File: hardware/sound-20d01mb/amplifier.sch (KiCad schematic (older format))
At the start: 43 parts

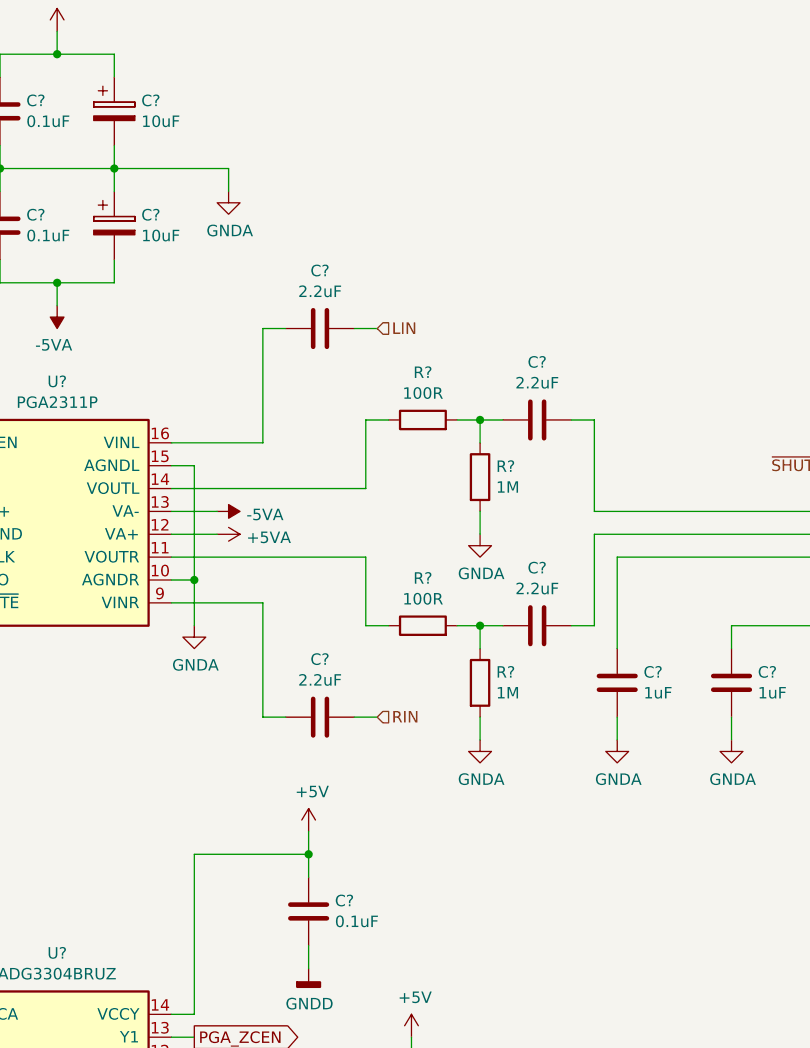
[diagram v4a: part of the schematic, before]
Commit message: Updated amplifier.sch
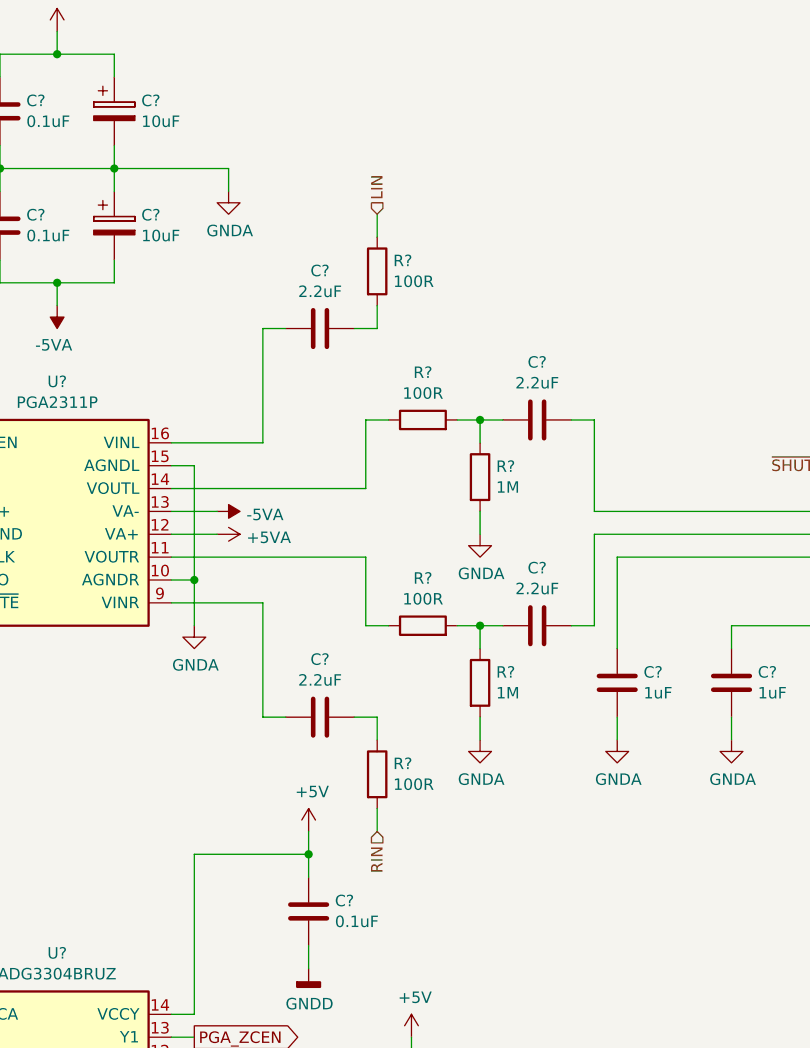
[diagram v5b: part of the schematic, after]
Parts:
- added R? (x2): 100R, Resistor_SMD:R_1206_3216Metric_Pad1.42x1.75mm_HandSolder, symbol Device:R
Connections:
- net LIN: now also R?.1; no longer C?.2
- net RIN: now also R?.2; no longer C?.2
- new net: C?.2, R?.2
- new net: C?.2, R?.1
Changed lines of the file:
@@
 	0    -1   -1   0
 $EndComp
-Text HLabel 4150 2700 2    50   Input ~ 0
+Text HLabel 4150 2200 1    50   Input ~ 0
 LIN
-Text HLabel 4150 4400 2    50   Input ~ 0
+Text HLabel 4150 4900 3    50   Input ~ 0
 RIN
 Text HLabel 10350 3000 2    50   Output ~ 0
@@
 	3650 4400 3750 4400
 Wire Wire Line
-	4150 2700 4050 2700
-Wire Wire Line
-	4150 4400 4050 4400
-Wire Wire Line
 	3250 3400 4100 3400
 Wire Wire Line
@@
 Wire Wire Line
 	5100 3600 6450 3600
+$Comp
+L Device:R R?
+U 1 1 60E82F70
+P 4150 2450
+F 0 "R?" H 4220 2496 50  0000 L CNN
+F 1 "100R" H 4220 2405 50  0000 L CNN
+F 2 "Resistor_SMD:R_1206_3216Metric_Pad1.42x1.75mm_HandSolder" V 4080 2450 50  0001 C CNN
+F 3 "~" H 4150 2450 50  0001 C CNN
+	1    4150 2450
+	1    0    0    -1
+$EndComp
+Wire Wire Line
+	4150 2200 4150 2300
+Wire Wire Line
+	4150 2600 4150 2700
+Wire Wire Line
+	4150 2700 4050 2700
+$Comp
+L Device:R R?
+U 1 1 60E9DE19
+P 4150 4650
+F 0 "R?" H 4220 4696 50  0000 L CNN
+F 1 "100R" H 4220 4605 50  0000 L CNN
+F 2 "Resistor_SMD:R_1206_3216Metric_Pad1.42x1.75mm_HandSolder" V 4080 4650 50  0001 C CNN
+F 3 "~" H 4150 4650 50  0001 C CNN
+	1    4150 4650
+	1    0    0    -1
+$EndComp
+Wire Wire Line
+	4150 4900 4150 4800
+Wire Wire Line
+	4150 4500 4150 4400
+Wire Wire Line
+	4150 4400 4050 4400
 $EndSCHEMATC

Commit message: THT to SMD Capacitor (2)
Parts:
- C?: footprint Capacitor_THT:CP_Radial_D8.0mm_P3.50mm -> Capacitor_SMD:CP_Elec_4x5.4
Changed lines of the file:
@@
 F 0 "C?" H 1268 2296 50  0000 L CNN
 F 1 "10uF" H 1268 2205 50  0000 L CNN
-F 2 "Capacitor_THT:CP_Radial_D8.0mm_P3.50mm" H 1188 2100 50  0001 C CNN
+F 2 "Capacitor_SMD:CP_Elec_4x5.4" H 1188 2100 50  0001 C CNN
 F 3 "~" H 1150 2250 50  0001 C CNN
 	1    1150 2250

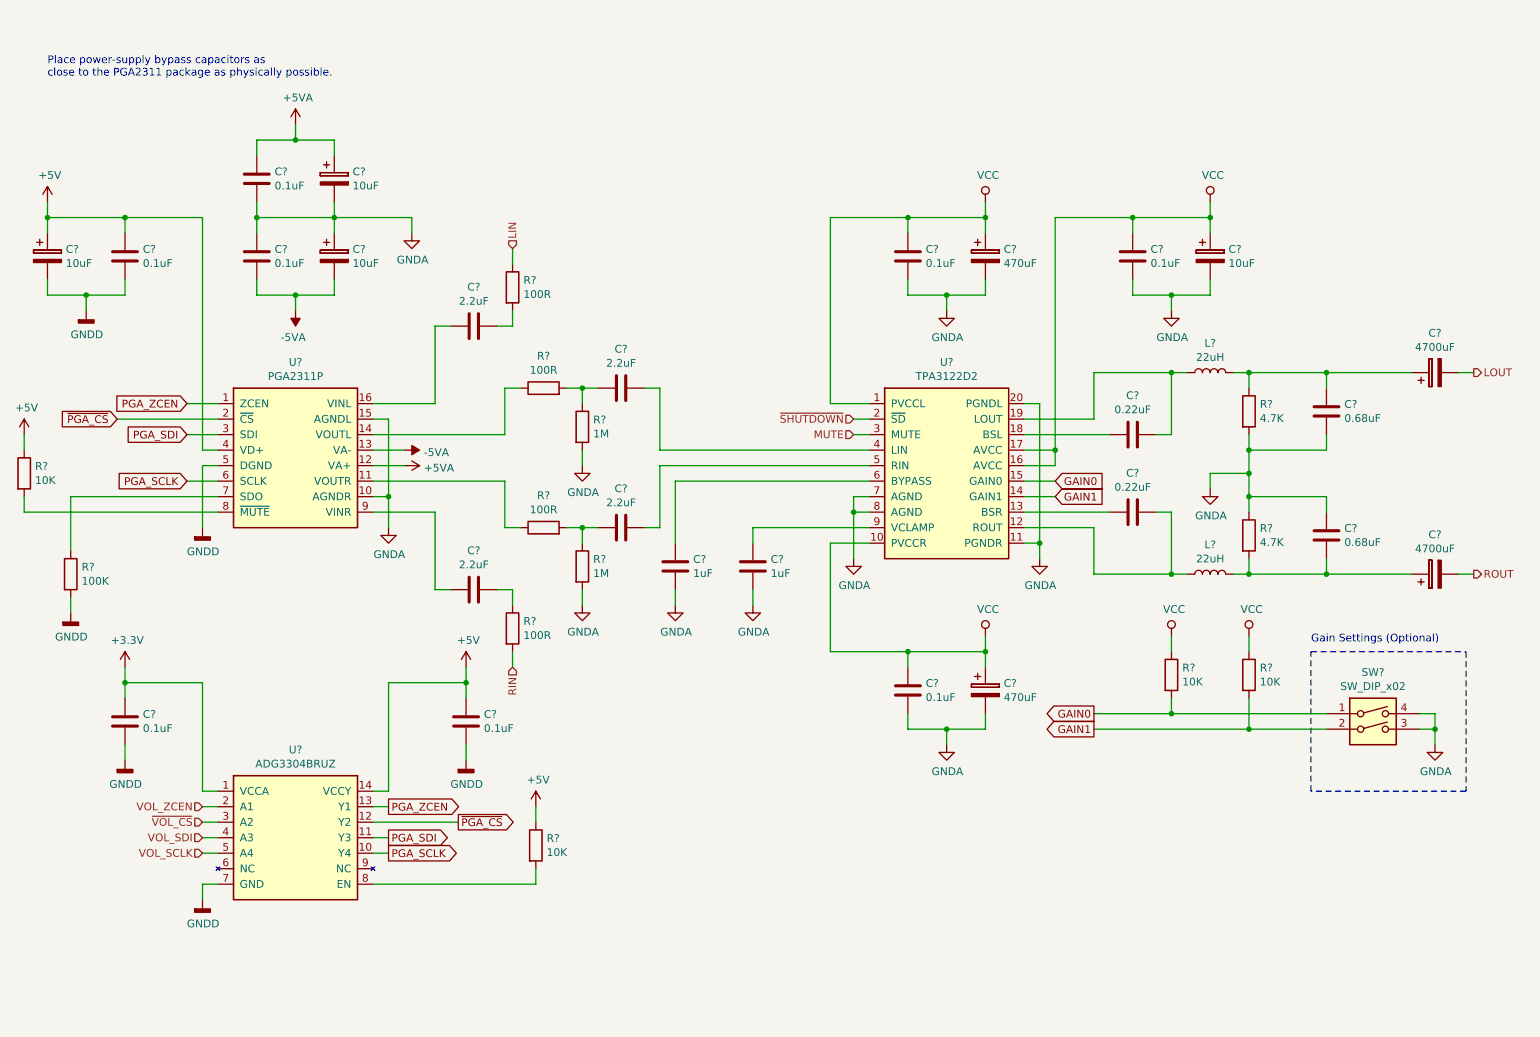
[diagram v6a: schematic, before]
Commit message: Added PC817
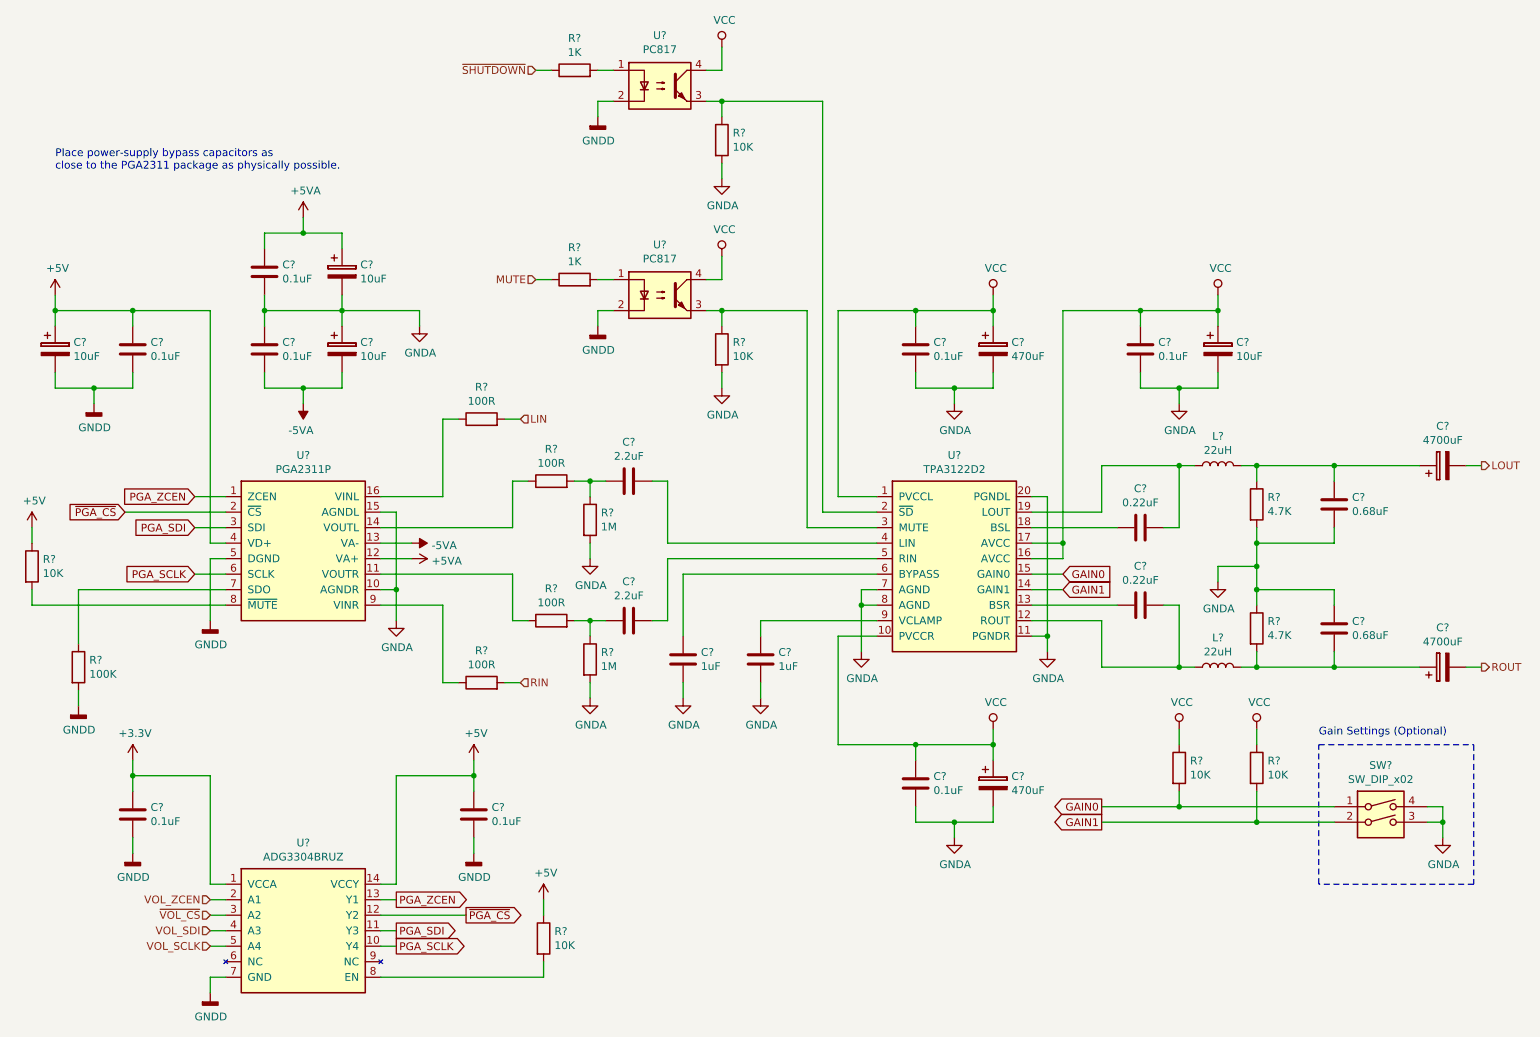
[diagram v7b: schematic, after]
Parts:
- removed C? (x2): 2.2uF, Capacitor_SMD:C_1206_3216Metric_Pad1.42x1.75mm_HandSolder, symbol Device:C
- removed R? (x2): 100R, Resistor_SMD:R_1206_3216Metric_Pad1.42x1.75mm_HandSolder, symbol Device:R
- added R? (x2): 10K, Resistor_SMD:R_1206_3216Metric_Pad1.42x1.75mm_HandSolder, symbol Device:R
- added R? (x2): 1K, Resistor_SMD:R_1206_3216Metric_Pad1.42x1.75mm_HandSolder, symbol Device:R
- added R? (x2): 100R, Resistor_SMD:R_1206_3216Metric_Pad1.42x1.75mm_HandSolder, symbol Device:R
- added U? (x2): PC817, Package_DIP:DIP-4_W7.62mm, symbol Isolator:PC817
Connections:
- net GNDA: now also R?.2, R?.2
- net GNDD: now also U?.2, U?.2
- net LIN: now also R?.2
- net MUTE: now also R?.1; no longer U?.3 (MUTE)
- net RIN: now also R?.2
- net VCC: now also U?.4, U?.4
- net ~SHUTDOWN: now also R?.1; no longer U?.2 (~SD)
- net at U?.16 (VINL): now also R?.1
- net at U?.9 (VINR): now also R?.1
- new net: R?.1, U?.2 (~SD), U?.3
- new net: R?.1, U?.3, U?.3 (MUTE)
- new net: R?.2, U?.1 (x2)
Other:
- moved on the sheet: C?, L?, R?, SW?, U?

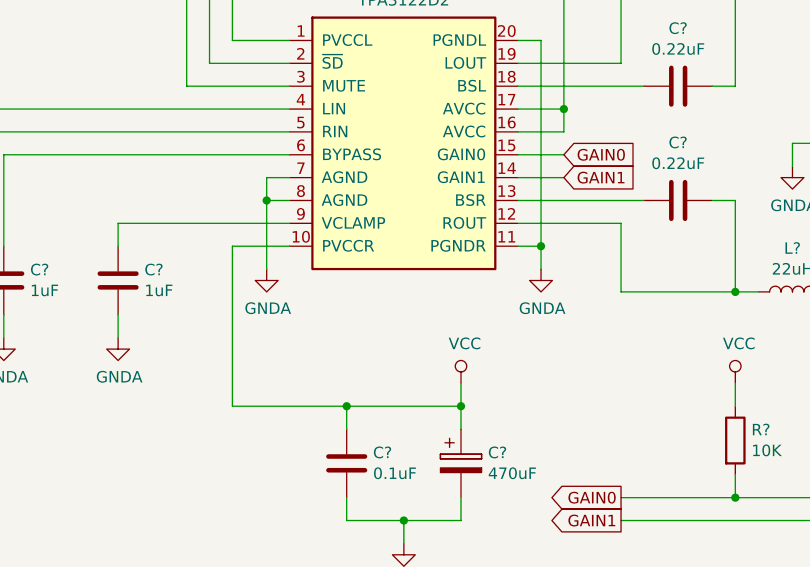
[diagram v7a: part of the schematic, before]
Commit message: Added oscillators sheet
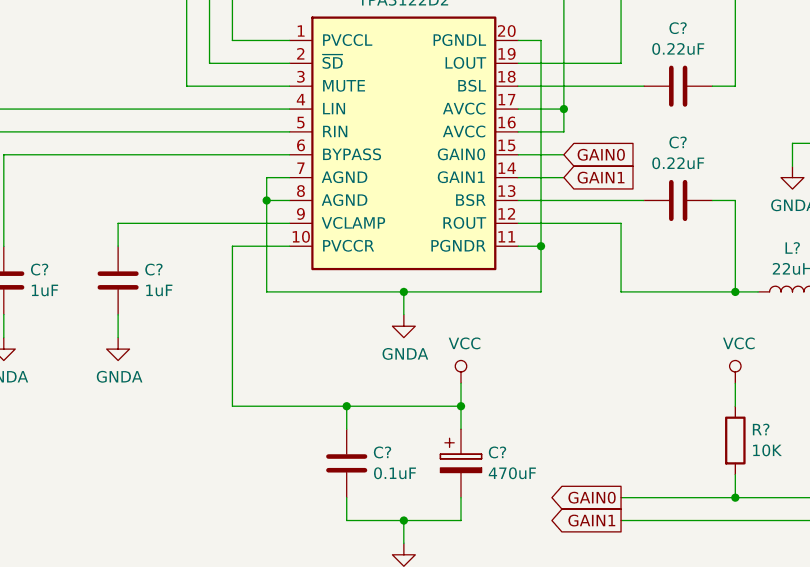
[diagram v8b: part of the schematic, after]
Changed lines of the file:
@@
 $Descr A4 11693 8268
 encoding utf-8
-Sheet 4 5
+Sheet 5 6
 Title "Sound-20D01MB"
 Date "2021-07-01"
@@
 L power:GNDA #PWR?
 U 1 1 60E18B79
-P 7600 4800
-F 0 "#PWR?" H 7600 4550 50  0001 C CNN
-F 1 "GNDA" H 7605 4627 50  0000 C CNN
-F 2 "" H 7600 4800 50  0001 C CNN
-F 3 "" H 7600 4800 50  0001 C CNN
-	1    7600 4800
+P 7000 5000
+F 0 "#PWR?" H 7000 4750 50  0001 C CNN
+F 1 "GNDA" H 7005 4827 50  0000 C CNN
+F 2 "" H 7000 5000 50  0001 C CNN
+F 3 "" H 7000 5000 50  0001 C CNN
+	1    7000 5000
 	1    0    0    -1
 $EndComp
 Wire Wire Line
 	7500 4700 7600 4700
-Wire Wire Line
-	7600 4700 7600 4800
 Wire Wire Line
 	7500 3800 7600 3800
@@
 Wire Wire Line
 	5250 4300 5250 4700
-Connection ~ 7600 4700
 Wire Wire Line
 	6500 4300 5250 4300
-$Comp
-L power:GNDA #PWR?
-U 1 1 60E61F4D
-P 6400 4800
-F 0 "#PWR?" H 6400 4550 50  0001 C CNN
-F 1 "GNDA" H 6405 4627 50  0000 C CNN
-F 2 "" H 6400 4800 50  0001 C CNN
-F 3 "" H 6400 4800 50  0001 C CNN
-	1    6400 4800
-	1    0    0    -1
-$EndComp
 Wire Wire Line
 	6500 4400 6400 4400
@@
 	6500 4500 6400 4500
 Connection ~ 6400 4500
-Wire Wire Line
-	6400 4500 6400 4800
 $Comp
 L Device:C C?
@@
 Wire Wire Line
 	4200 5000 4100 5000
+Connection ~ 7600 4700
+Wire Wire Line
+	7600 4900 7000 4900
+Wire Wire Line
+	7000 4900 7000 5000
+Wire Wire Line
+	7600 4700 7600 4900
+Wire Wire Line
+	6400 4900 7000 4900
+Wire Wire Line
+	6400 4500 6400 4900
+Connection ~ 7000 4900
 $EndSCHEMATC
